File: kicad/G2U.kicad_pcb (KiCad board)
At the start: 2 copper layers, 78 x 71.4 mm, 38 parts, among them J1 Conn_02x12_Counter_Clockwise_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

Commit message: Final 0603 board
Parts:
- removed the REF** at (197.2, 34.1)
- removed the REF** at (197.2, 97.7)
- R1, R10, R11, R12, R13, R14, R15, R16, R17, R18, R19, R2, R20, R21, R22, R23, R24, R25, R26, R27, R28, R29, R3, R30, R31, R32, R4, R5, R6, R7, R8, R9: footprint Resistor_THT:R_Axial_DIN0207_L6.3mm_D2.5mm_P10.16mm_Horizontal -> Resistor_SMD:R_0603_1608Metric_Pad0.98x0.95mm_HandSolder
- moved R32 118.5 mm to (104.8, 125.8)
- moved R30 117.9 mm to (104.8, 129.4)
- moved R16 107.5 mm to (97.7, 125.6)
- moved R14 106.9 mm to (97.7, 129.2)
- moved J1 82.5 mm to (114.9, 90.5)
- moved R23 81.2 mm to (104.7, 75.2)
- moved R24 80.8 mm to (104.8, 78.8)
- moved R25 80.6 mm to (104.8, 82.4)
- moved R26 80.3 mm to (104.8, 86.0)
- moved R27 80.0 mm to (104.8, 89.6)
- moved R28 79.8 mm to (104.8, 93.2)
- moved R29 79.5 mm to (104.8, 96.8)
- moved R31 77.8 mm to (104.8, 122.1)
- moved A1 70.3 mm to (71.9, 89.0)
- moved R20 69.9 mm to (104.8, 100.5)
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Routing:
- net Net-(A1-D11): track 85.9 -> 35.6 mm
- net Net-(A1-D8): track 84.4 -> 40.2 mm
- net Net-(A1-D7): track 81.9 -> 41.1 mm
- net Net-(A1-D9): track 79.8 -> 44.0 mm
- net Net-(A1-D6): track 77.1 -> 42.2 mm
- net GND: track 128.8 -> 97.0 mm
- net Net-(J1-Pin_16): track 70.0 -> 39.0 mm
- net Net-(A1-D5): track 73.0 -> 43.2 mm
- net Net-(A1-D4): track 68.6 -> 44.4 mm
- net Net-(J1-Pin_15): track 57.3 -> 33.8 mm
- net Net-(J1-Pin_14): track 51.1 -> 28.7 mm
- net Net-(A1-D3): track 64.7 -> 42.8 mm
- net Net-(A1-A5): track 57.3 -> 40.7 mm
- net Net-(A1-A4): track 49.9 -> 34.0 mm
- net Net-(J1-Pin_17): track 64.6 -> 49.7 mm
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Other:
- board size 78 x 71.4 mm -> 63.5 x 59.2 mm
- board text added: "(c) March 2026, Andrew Martin, Acramonics Original circuit: Rudolf Reuter; Adapted by: TheHWCave"
- board text added: "- All 120R -"
- board text added: "- All 6K2 -"
- board text added: "GPIB2USB V1.1"
- board text removed: "(c) March 2026 Andrew Martin Acramonics"
- board text removed: "GPIB2USB V1.0"
- board text removed: "Original circuit: Rudolf Reuter Adapted by: TheHWCave"
- board text removed: "R1 - R16 6K2 R17 - R32 120R"

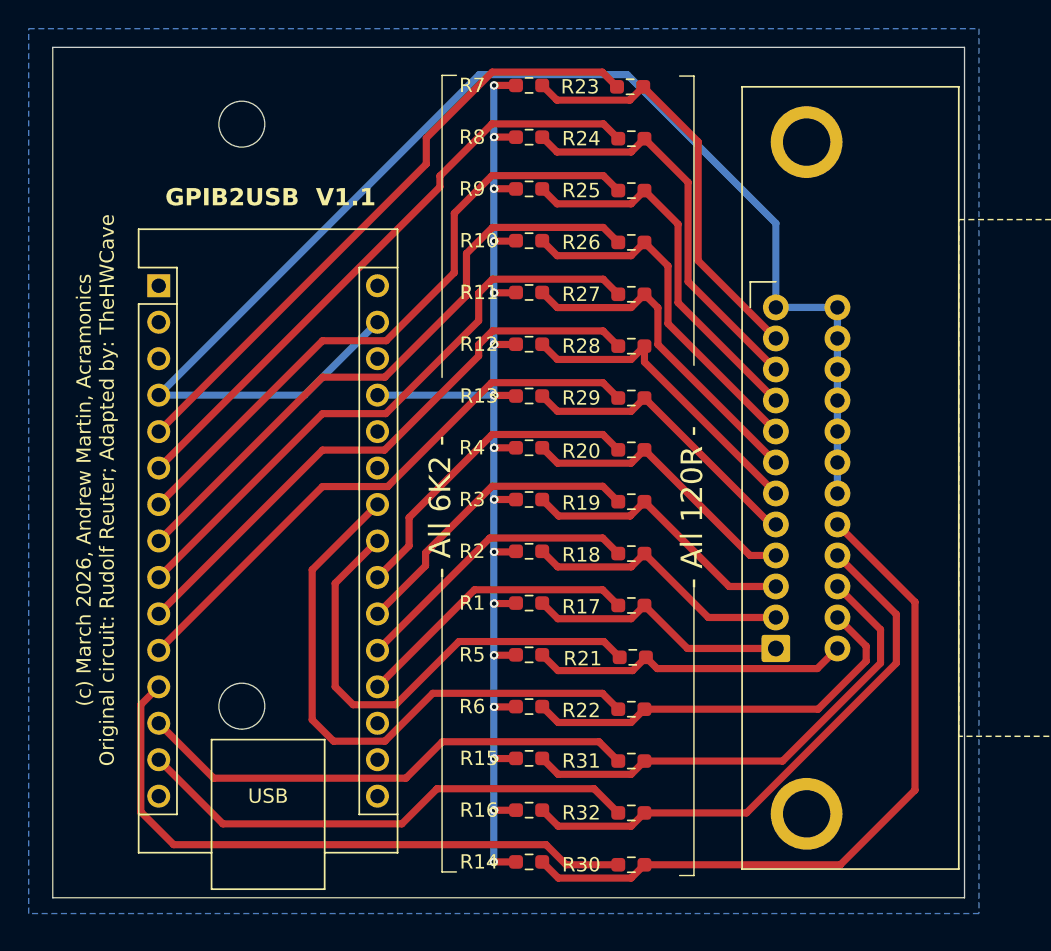
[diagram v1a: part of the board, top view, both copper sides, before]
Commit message: Changed to 1206 SMD and moved the Nano to the edge of the board
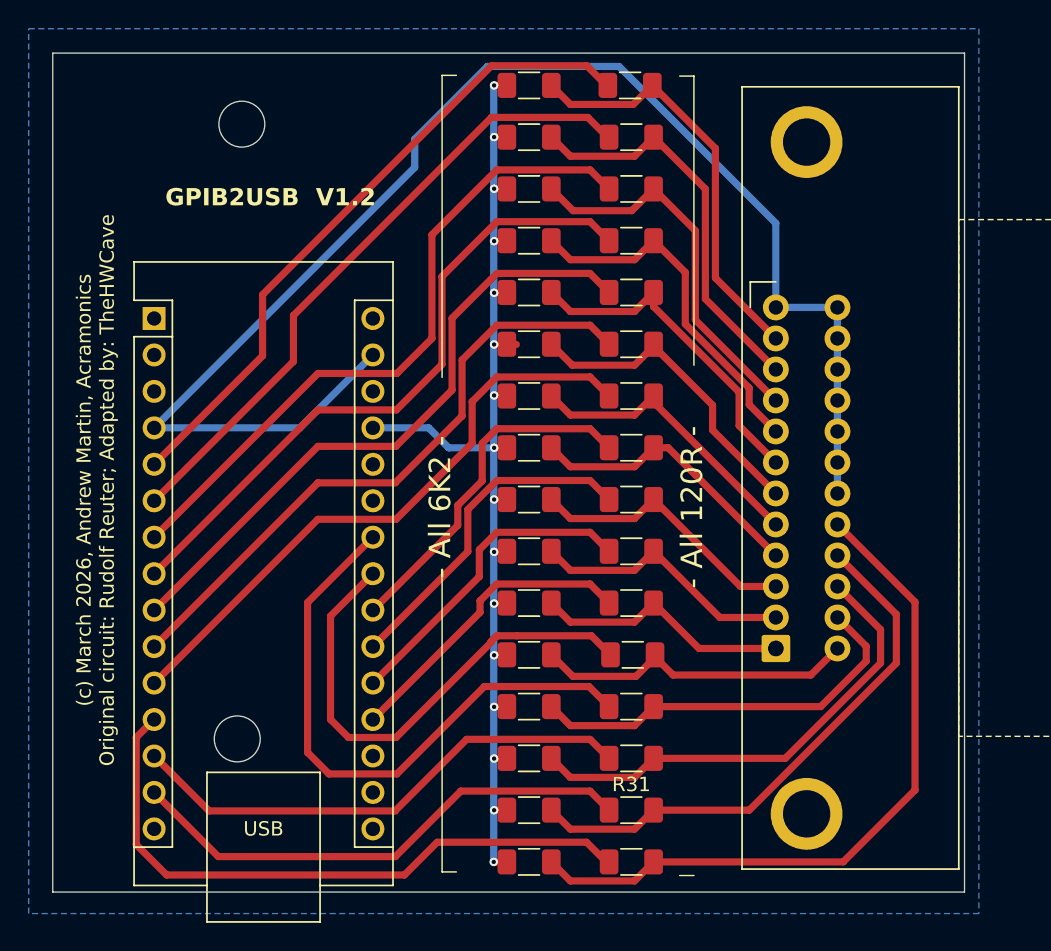
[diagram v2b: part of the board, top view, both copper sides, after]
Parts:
- R1, R10, R11, R12, R13, R14, R15, R16, R17, R18, R19, R2, R20, R21, R22, R23, R24, R25, R26, R27, R28, R29, R3, R30, R31, R32, R4, R5, R6, R7, R8, R9: footprint Resistor_SMD:R_0603_1608Metric_Pad0.98x0.95mm_HandSolder -> Resistor_SMD:R_1206_3216Metric_Pad1.30x1.75mm_HandSolder
- moved REF** 2.30 mm to (77.3, 120.6)
- moved A1 2.30 mm to (71.5, 91.3)
- moved R30 0.20 mm to (104.8, 129.2)
- moved R32 0.19 mm to (104.8, 125.6)
- moved R31 0.19 mm to (104.8, 122.0)
- moved R22 0.18 mm to (104.8, 118.3)
- moved R21 0.17 mm to (104.9, 114.7)
- moved R17 0.17 mm to (104.8, 111.1)
- moved R18 0.16 mm to (104.8, 107.5)
- moved R19 0.15 mm to (104.8, 103.9)
- moved R20 0.15 mm to (104.8, 100.3)
- moved R29 0.14 mm to (104.8, 96.7)
- moved R28 0.13 mm to (104.8, 93.1)
- moved R27 0.13 mm to (104.8, 89.5)
- moved R26 0.12 mm to (104.8, 85.9)
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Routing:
- net +5V: track 87.0 -> 79.1 mm
- net GND: track 97.0 -> 99.9 mm
- net Net-(A1-D5): track 43.2 -> 46.0 mm
- net Net-(A1-D7): track 41.1 -> 43.8 mm
- net Net-(A1-D4): track 44.4 -> 47.1 mm
- net Net-(A1-D6): track 42.2 -> 44.9 mm
- net Net-(A1-D8): track 40.2 -> 42.8 mm
- net Net-(A1-D3): track 42.8 -> 45.3 mm
- net Net-(A1-D2): track 43.8 -> 46.2 mm
- net Net-(A1-A3): track 22.5 -> 24.6 mm
- net Net-(A1-A2): track 21.4 -> 23.5 mm
- net Net-(A1-A1): track 20.5 -> 22.5 mm
- net Net-(A1-A0): track 20.0 -> 21.4 mm
- net Net-(A1-A5): track 40.7 -> 41.6 mm
- net Net-(A1-A4): track 34.0 -> 34.9 mm
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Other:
- board size 63.5 x 59.2 mm -> 63.5 x 58.5 mm
- board text added: "GPIB2USB V1.2"
- board text removed: "GPIB2USB V1.1"

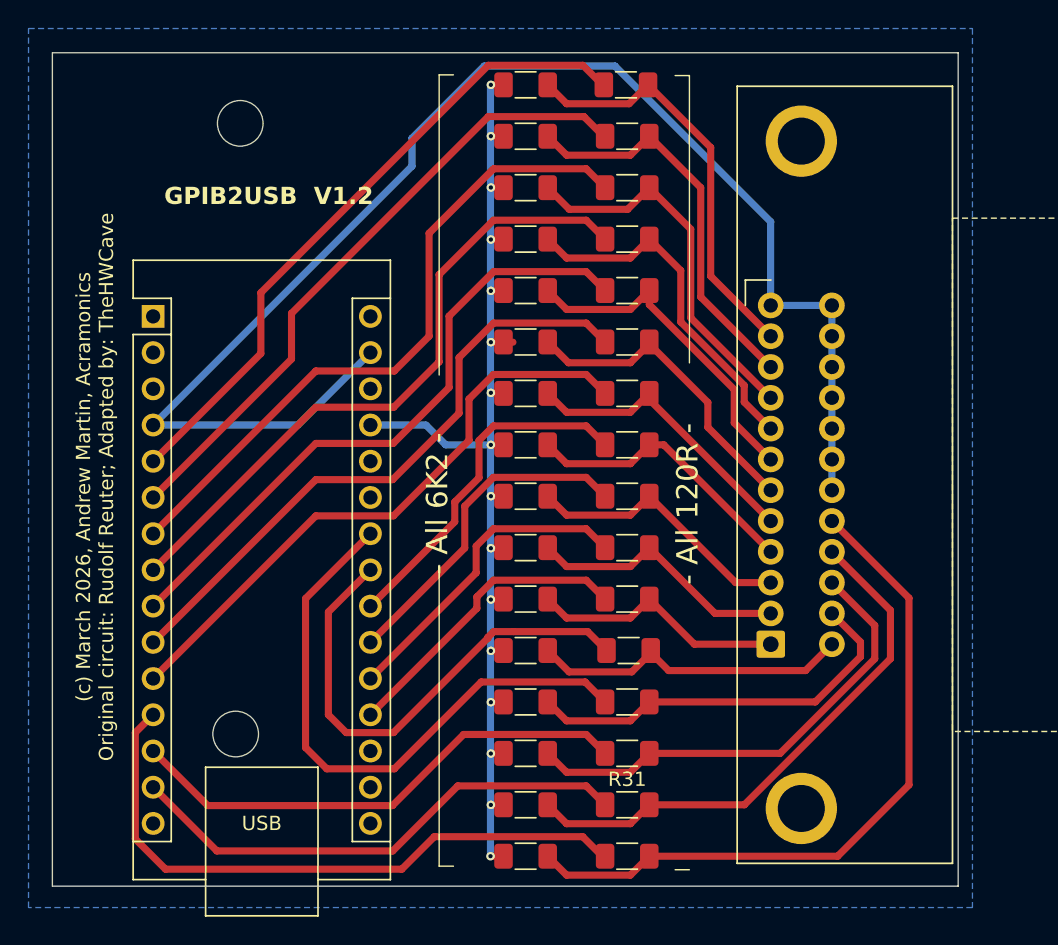
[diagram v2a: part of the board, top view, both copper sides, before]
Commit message: Shrunk board in y-direction
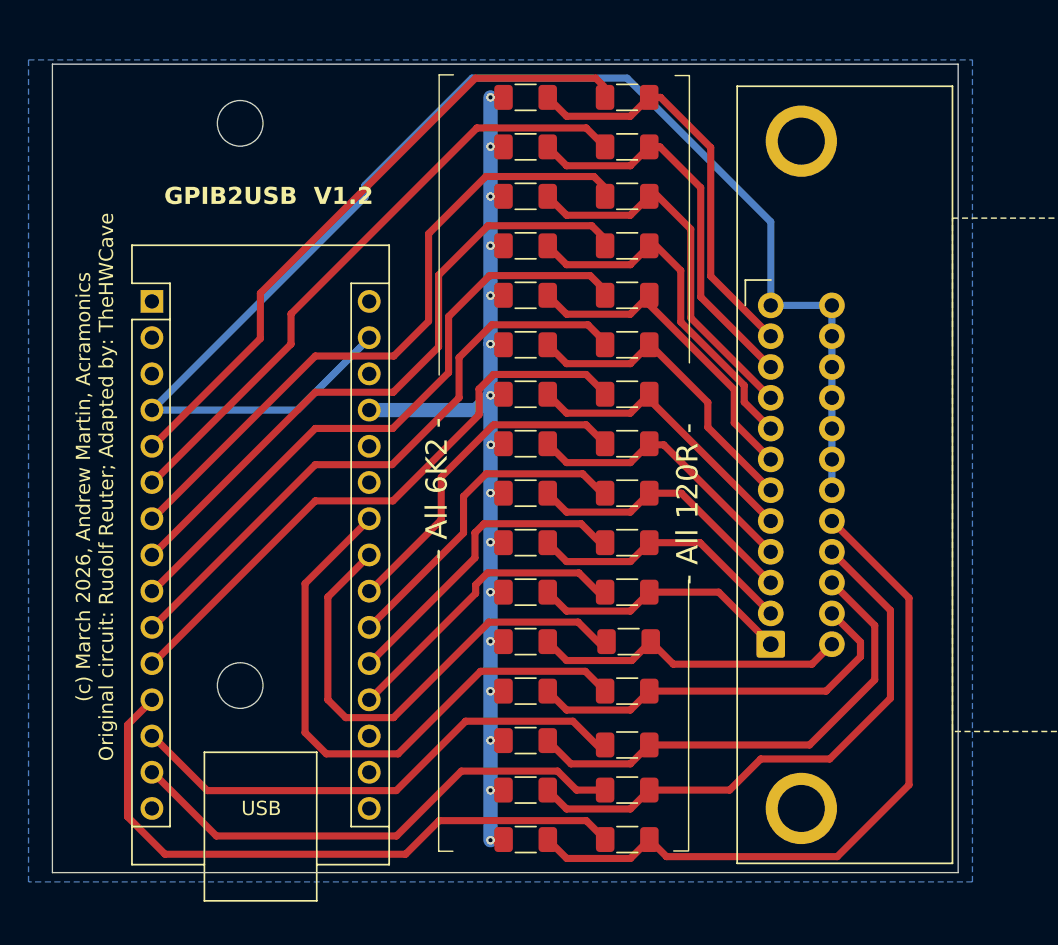
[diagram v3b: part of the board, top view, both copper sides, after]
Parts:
- moved REF** 3.41 mm to (77.7, 117.2)
- moved R14 1.17 mm to (97.7, 128.0)
- moved R30 1.17 mm to (104.8, 128.0)
- moved A1 1.05 mm to (71.5, 90.3)
- moved R16 1.03 mm to (97.7, 124.5)
- moved R32 1.03 mm to (104.8, 124.5)
- moved R15 0.90 mm to (97.7, 121.1)
- moved R23 0.88 mm to (104.8, 76.0)
- moved R7 0.88 mm to (97.7, 76.0)
- moved R22 0.76 mm to (104.8, 117.6)
- moved R6 0.76 mm to (97.7, 117.6)
- moved R24 0.74 mm to (104.8, 79.4)
- moved R8 0.74 mm to (97.7, 79.4)
- moved R21 0.62 mm to (104.9, 114.1)
- moved R5 0.62 mm to (97.7, 114.1)
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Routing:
- net +5V: track 79.1 -> 76.0 mm
- net Net-(A1-D2): track 46.2 -> 44.4 mm
- net GND: track 99.9 -> 98.2 mm
- net Net-(A1-D4): track 47.1 -> 45.6 mm
- net Net-(A1-D3): track 45.3 -> 43.8 mm
- net Net-(A1-D5): track 46.0 -> 44.6 mm
- net Net-(A1-D6): track 44.9 -> 43.6 mm
- net Net-(J1-Pin_16): track 38.6 -> 39.8 mm
- net Net-(A1-D7): track 43.8 -> 42.7 mm
- net Net-(A1-D8): track 42.8 -> 41.7 mm
- net Net-(A1-A3): track 24.6 -> 23.6 mm
- net Net-(J1-Pin_15): track 33.4 -> 34.1 mm
- net Net-(J1-Pin_17): track 49.3 -> 49.8 mm
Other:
- board size 63.5 x 58.5 mm -> 63.5 x 56.7 mm

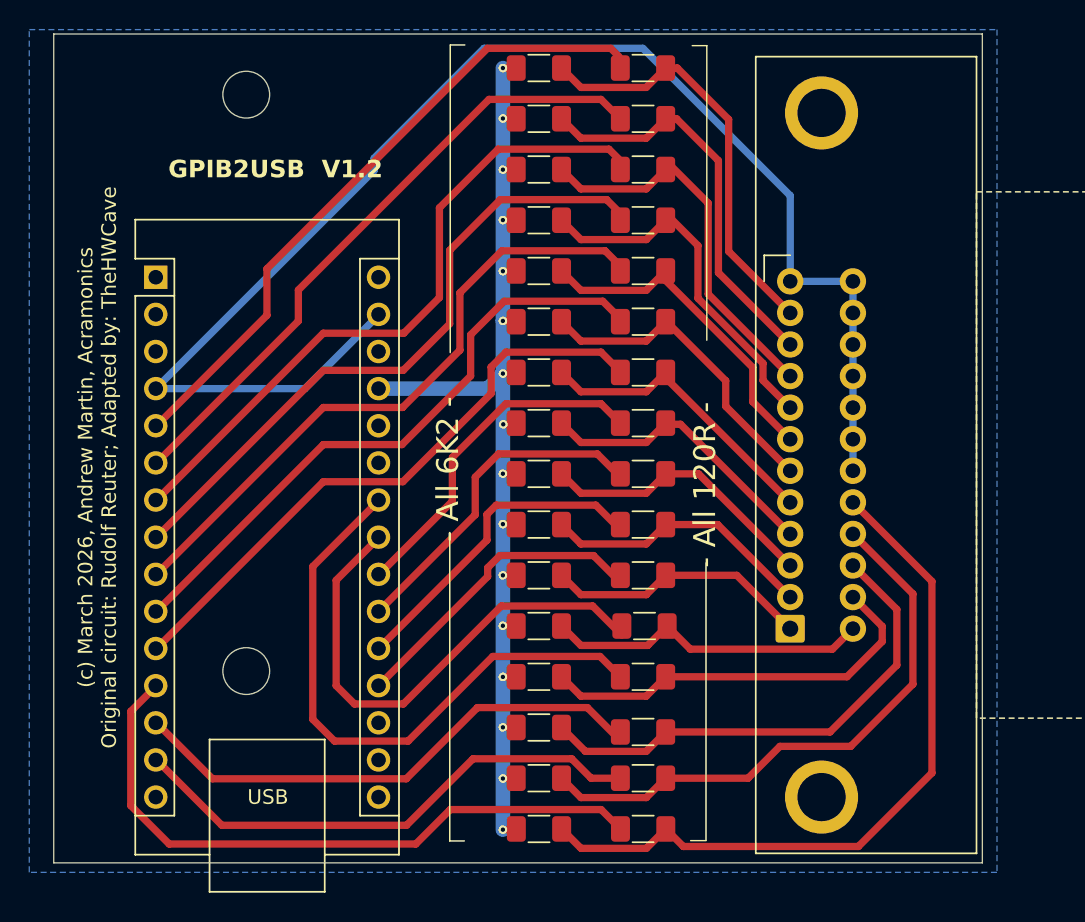
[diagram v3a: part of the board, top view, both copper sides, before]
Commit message: A bit more shrinking and regenerated gerber files
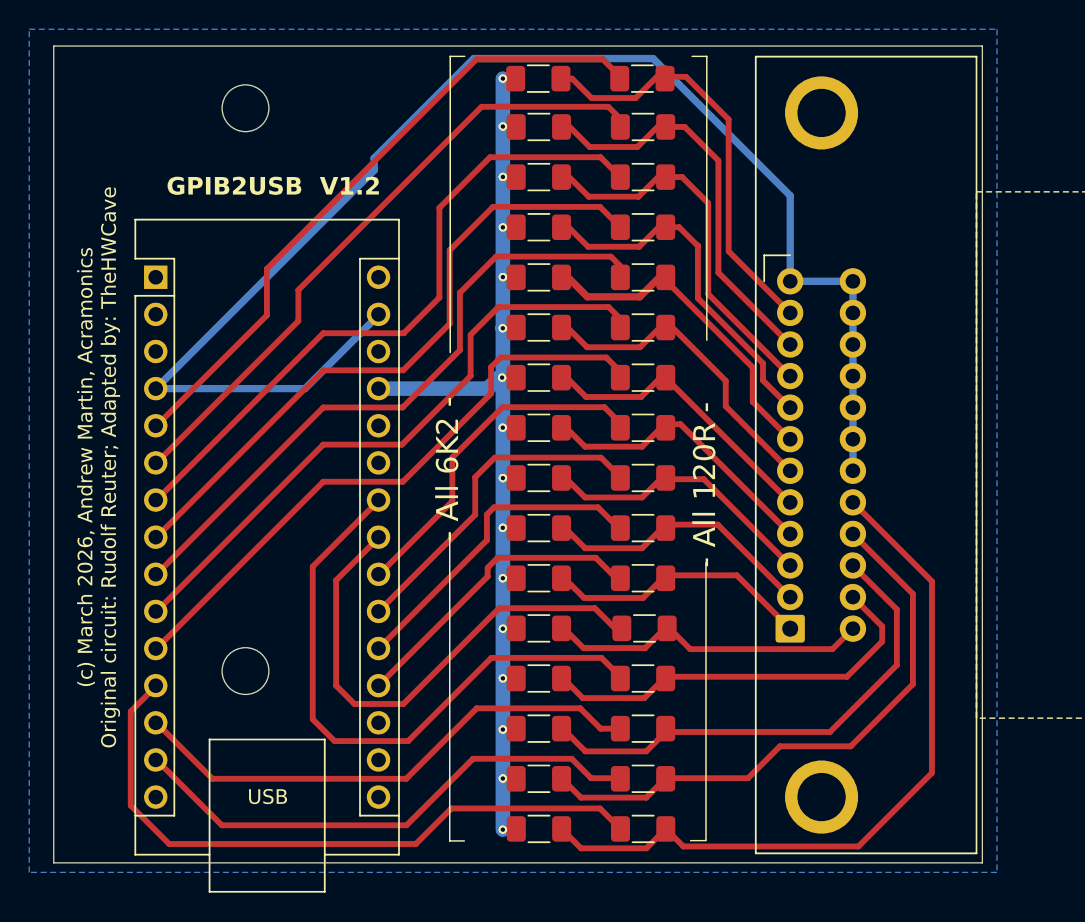
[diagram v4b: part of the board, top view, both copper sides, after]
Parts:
- moved REF** 0.93 mm to (77.6, 78.7)
- moved R7 0.73 mm to (97.6, 76.7)
- moved R23 0.73 mm to (104.8, 76.7)
- moved R24 0.56 mm to (104.8, 80.0)
- moved R8 0.56 mm to (97.7, 80.0)
- moved R25 0.52 mm to (104.8, 83.4)
- moved R9 0.52 mm to (97.7, 83.4)
- moved R10 0.48 mm to (97.7, 86.8)
- moved R26 0.48 mm to (104.8, 86.8)
- moved R11 0.44 mm to (97.7, 90.3)
- moved R27 0.44 mm to (104.8, 90.3)
- moved R12 0.40 mm to (97.7, 93.7)
- moved R28 0.40 mm to (104.8, 93.7)
- moved R13 0.36 mm to (97.7, 97.1)
- moved R29 0.36 mm to (104.8, 97.1)
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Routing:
- net Net-(J1-Pin_7): track 23.6 -> 23.0 mm
- net GND: track 98.2 -> 97.6 mm
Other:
- board size 63.5 x 56.7 mm -> 63.5 x 55.9 mm
